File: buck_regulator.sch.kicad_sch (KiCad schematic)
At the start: 4 parts, among them U1 XL1509-12

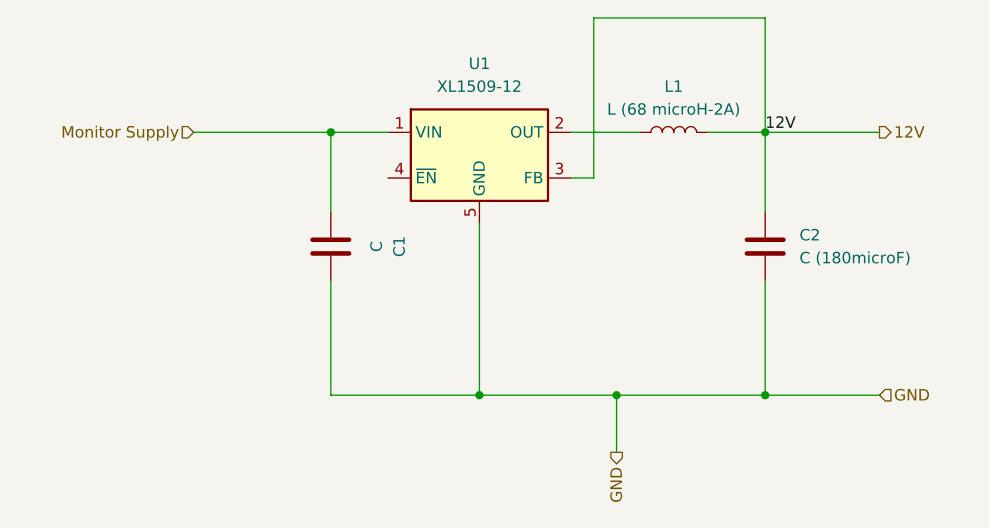
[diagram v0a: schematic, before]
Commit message: Update Hall Sensor
Swapped Bilateral for Unilateral hall sensor and added Hierarchy. Added Load tags
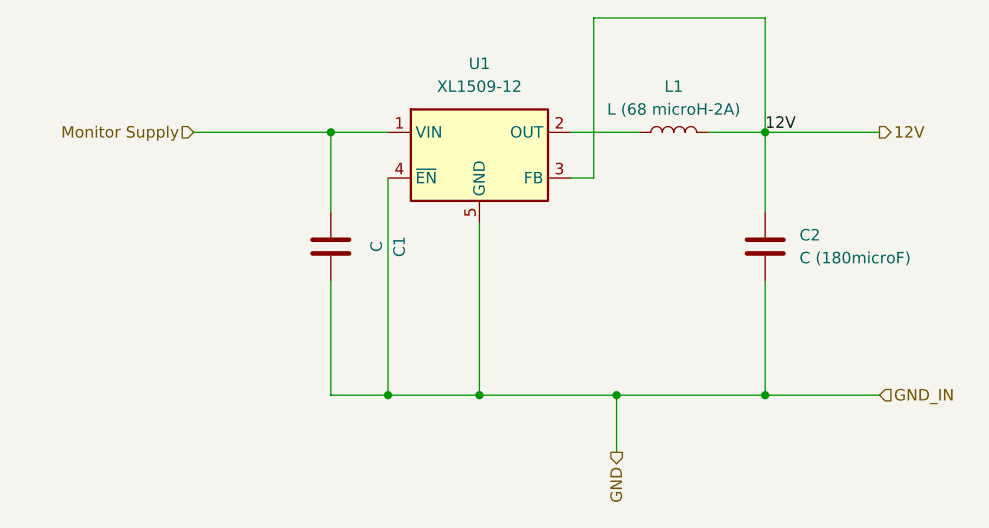
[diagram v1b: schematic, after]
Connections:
- net GND: now also U1.4 (~{EN})
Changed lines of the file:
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@@
+	)
+	(junction
+		(at 118.11 107.95)
+		(diameter 0)
+		(color 0 0 0 0)
 	)
 	(junction
@@
 	(wire
 		(pts
+			(xy 118.11 107.95) (xy 128.27 107.95)
+		)
+		(stroke
+			(width 0)
+			(type default)
+		)
+	)
+	(wire
+		(pts
 			(xy 111.76 78.74) (xy 111.76 87.63)
 		)
@@
 	(wire
 		(pts
+			(xy 118.11 83.82) (xy 118.11 107.95)
+		)
+		(stroke
+			(width 0)
+			(type default)
+		)
+	)
+	(wire
+		(pts
 			(xy 160.02 66.04) (xy 160.02 78.74)
 		)
@@
 	(wire
 		(pts
-			(xy 111.76 107.95) (xy 128.27 107.95)
+			(xy 111.76 107.95) (xy 118.11 107.95)
 		)
 		(stroke
@@
 		)
 	)
-	(hierarchical_label "GND"
+	(hierarchical_label "GND_IN"
 		(shape input)
 		(at 172.72 107.95 0)
